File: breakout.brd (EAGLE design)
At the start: 60.6 x 19 mm, 3 parts, among them X1 SCART-F

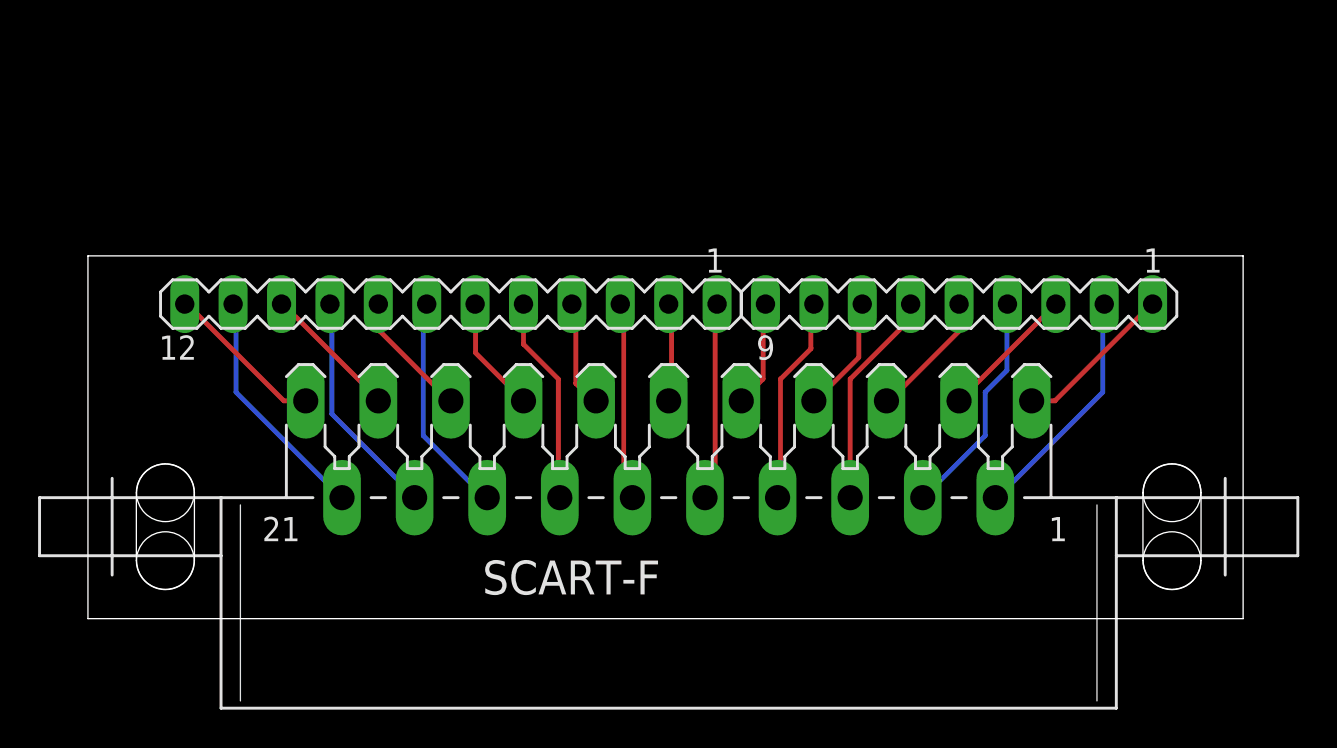
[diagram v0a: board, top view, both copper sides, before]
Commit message: Version 2 of the breakout board
- Created a 21-pin header part instead of using 9 & 12-pin parts
- Routed all the wires manually on the bottom layer
- Added the pinouts as documented on Wikipedia to the top layer at the
  expense of making the board slightly bigger
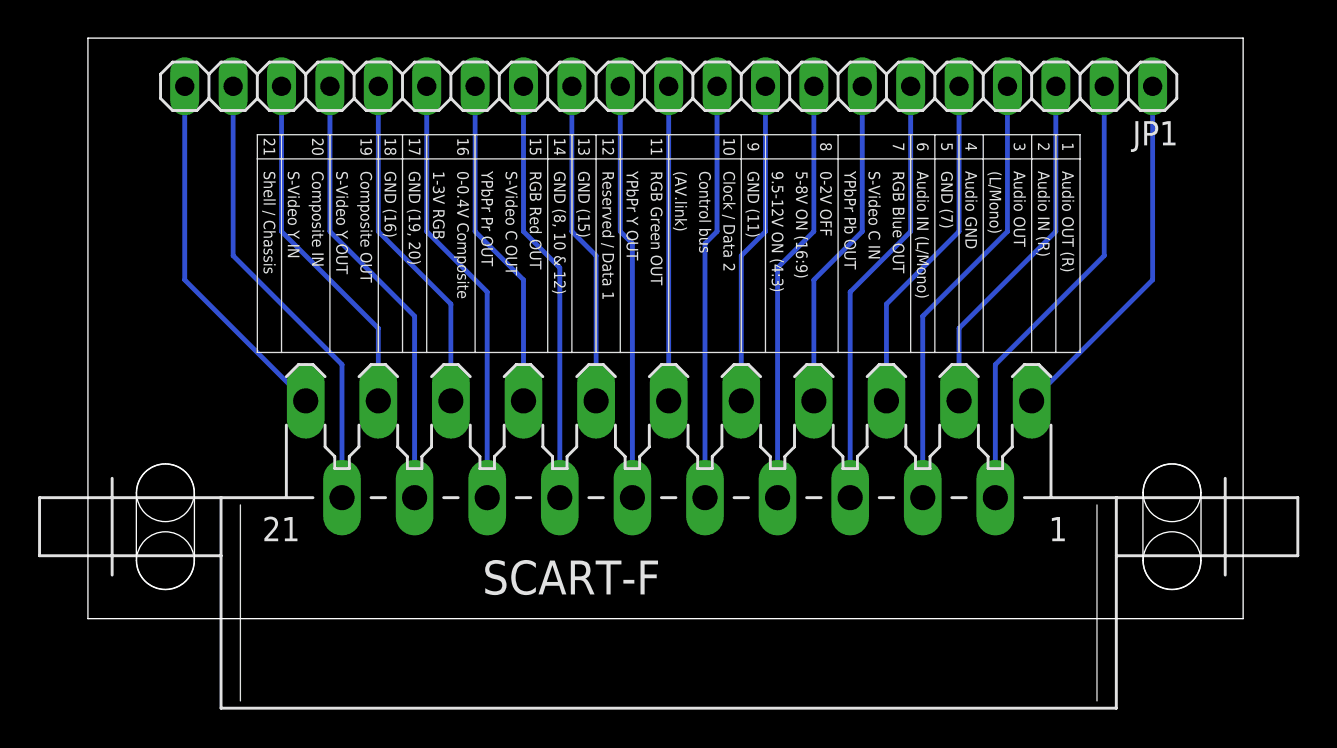
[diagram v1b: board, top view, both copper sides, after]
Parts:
- removed SV1: (no value), con-lstb:MA12-1
- removed SV2: (no value), con-lstb:MA09-1
- added JP1: (no value), pinhead:1X21
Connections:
- net N$1: now also JP1.10, X1.10; no longer SV2.1, X1.1
- net N$10: now also JP1.20, X1.20; no longer SV1.1, X1.10
- net N$11: now also JP1.21, X1.21; no longer SV1.2, X1.11
- net N$12: now also JP1.19, X1.19; no longer SV1.3, X1.12
- net N$13: now also JP1.17, X1.17; no longer SV1.4, X1.13
- net N$14: now also JP1.15, X1.15; no longer SV1.5, X1.14
- net N$15: now also JP1.13, X1.13; no longer SV1.6, X1.15
- net N$16: now also JP1.11, X1.11; no longer SV1.7, X1.16
- net N$17: now also JP1.9, X1.9; no longer SV1.8, X1.17
- net N$18: now also JP1.7, X1.7; no longer SV1.9, X1.18
- net N$19: now also JP1.5, X1.5; no longer SV1.10, X1.19
- net N$2: now also JP1.12, X1.12; no longer SV2.2, X1.2
- net N$20: now also JP1.3, X1.3; no longer SV1.11, X1.20
- net N$21: now also JP1.1, X1.1; no longer SV1.12, X1.21
- net N$3: now also JP1.8, X1.8; no longer SV2.3, X1.3
- net N$4: now also JP1.6, X1.6; no longer SV2.4, X1.4
- net N$5: now also JP1.4, X1.4; no longer SV2.5, X1.5
- net N$6: now also JP1.2, X1.2; no longer SV2.6, X1.6
- net N$7: now also JP1.14, X1.14; no longer SV2.7, X1.7
- net N$8: now also JP1.16, X1.16; no longer SV2.8, X1.8
- net N$9: now also JP1.18, X1.18; no longer SV2.9, X1.9
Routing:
- net N$9: track 5.64 -> 23.4 mm
- net N$5: track 6.75 -> 23.4 mm
- net N$7: track 6.24 -> 22.4 mm
- net N$3: track 7.18 -> 22.4 mm
- net N$11: track 5.34 -> 19.1 mm
- net N$10: track 10.5 -> 24.0 mm
- net N$1: track 8.45 -> 21.9 mm
- net N$6: track 11.5 -> 24.0 mm
- net N$13: track 5.77 -> 18.1 mm
- net N$8: track 11.0 -> 22.9 mm
- net N$15: track 6.13 -> 17.0 mm
- net N$4: track 12.0 -> 22.9 mm
- net N$19: track 7.33 -> 18.1 mm
- net N$21: track 8.44 -> 19.1 mm
- net N$17: track 6.71 -> 17.0 mm
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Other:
- board size 60.6 x 19 mm -> 60.6 x 30.5 mm
- board text added: "(AV.link)"
- board text added: "(L/Mono)"
- board text added: "0-0.4V Composite"
- board text added: "0-2V OFF"
- board text added: "1"
- board text added: "1-3V RGB"
- board text added: "10"
- board text added: "11"
- board text added: "12"
- board text added: "13"
- board text added: "14"
- board text added: "15"
- board text added: "16"
- board text added: "17"
- board text added: "18"
- board text added: "19"
- board text added: "2"
- board text added: "20"
- board text added: "21"
- board text added: "3"
- board text added: "4"
- board text added: "5"
- board text added: "5-8V ON (16:9)"
- board text added: "6"
- board text added: "7"
- board text added: "8"
- board text added: "9"
- board text added: "9.5-12V ON (4:3)"
- board text added: "Audio GND"
- board text added: "Audio IN (L/Mono)"
- board text added: "Audio IN (R)"
- board text added: "Audio OUT"
- board text added: "Audio OUT (R)"
- board text added: "Clock / Data 2"
- board text added: "Composite IN"
- board text added: "Composite OUT"
- board text added: "Control bus"
- board text added: "GND (11)"
- board text added: "GND (15)"
- board text added: "GND (16)"
- board text added: "GND (19, 20)"
- board text added: "GND (7)"
- board text added: "GND (8, 10 & 12)"
- board text added: "RGB Blue OUT"
- board text added: "RGB Green OUT"
- board text added: "RGB Red OUT"
- board text added: "Reserved / Data 1"
- board text added: "S-Video C IN"
- board text added: "S-Video C OUT"
- board text added: "S-Video Y IN"
- board text added: "S-Video Y OUT"
- board text added: "Shell / Chassis"
- board text added: "YPbPr Pb OUT"
- board text added: "YPbPr Pr OUT"
- board text added: "YPbPr Y OUT"
